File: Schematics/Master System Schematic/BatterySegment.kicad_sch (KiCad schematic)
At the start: 148 parts

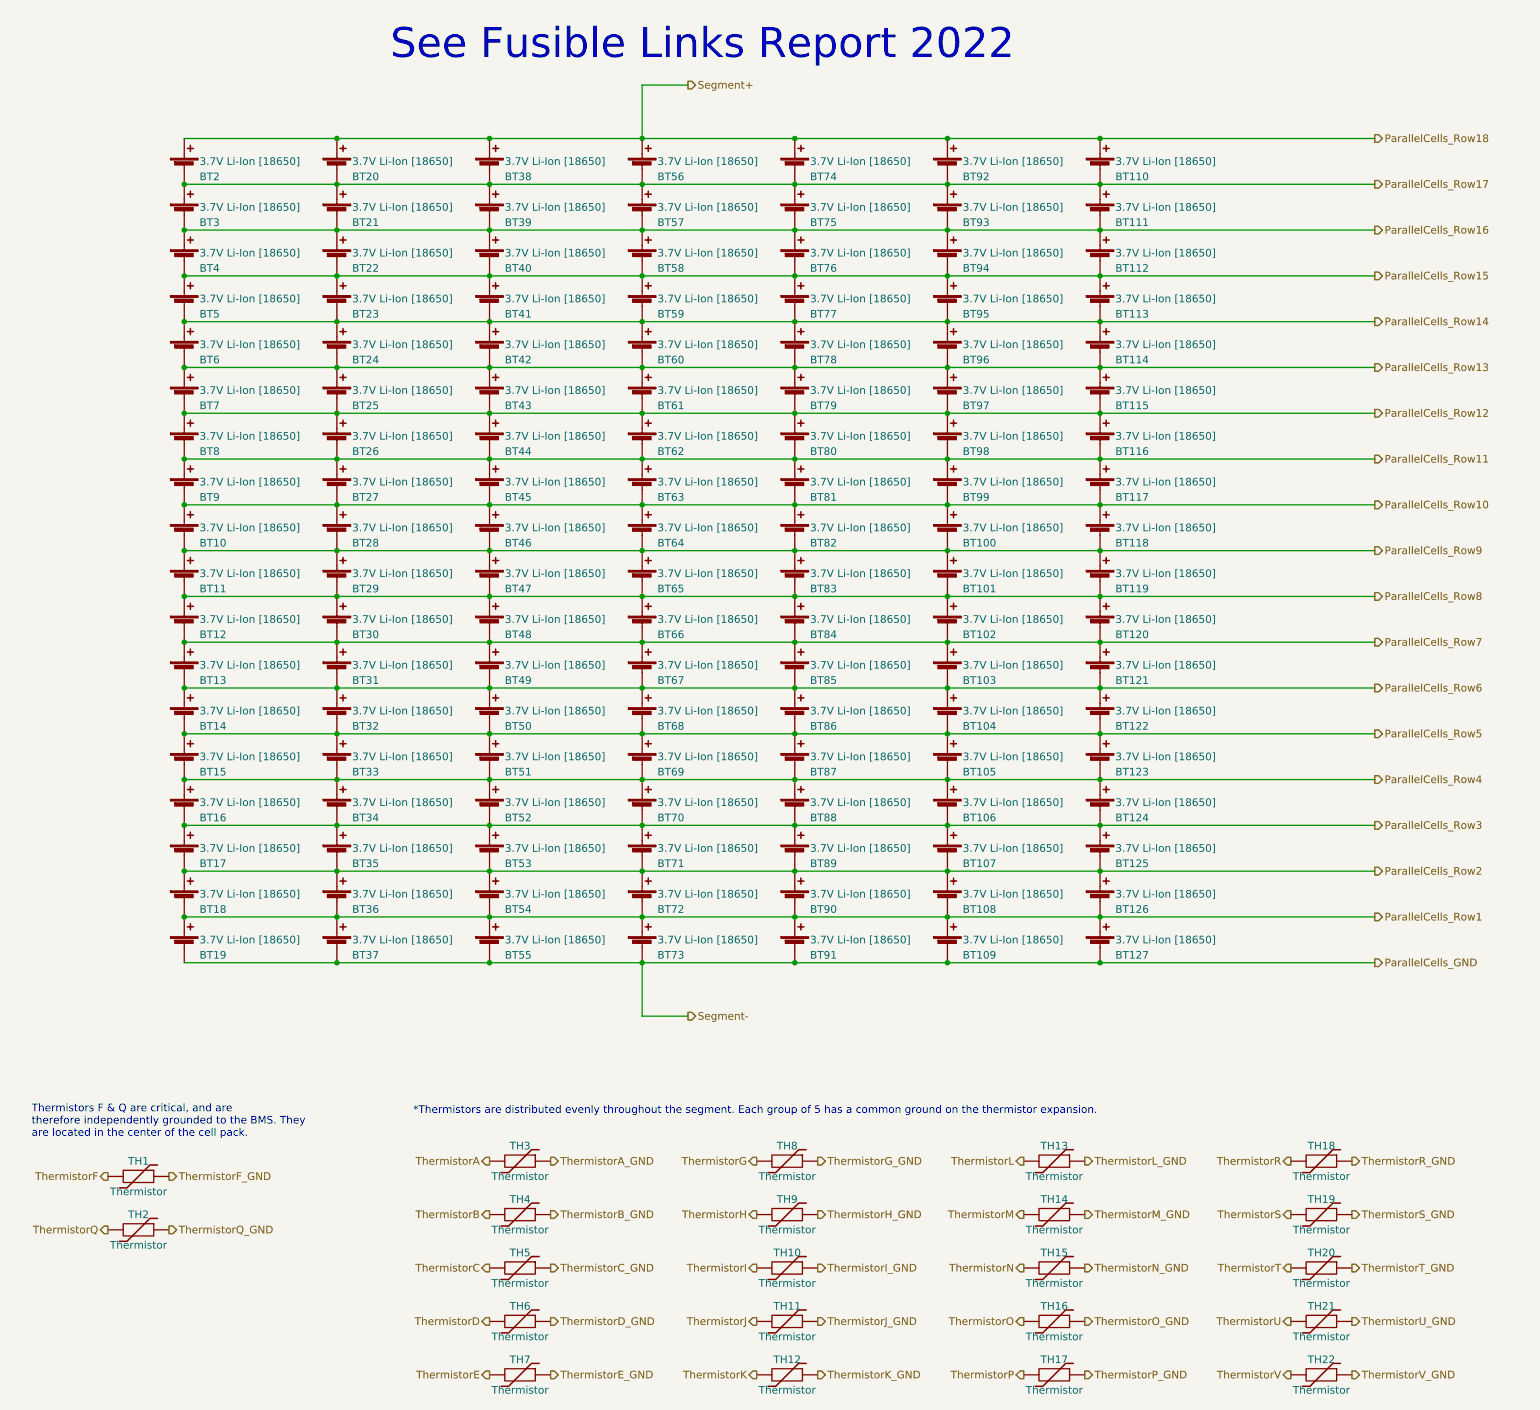
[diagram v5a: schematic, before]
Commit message: Update for color coding
Update for color coding
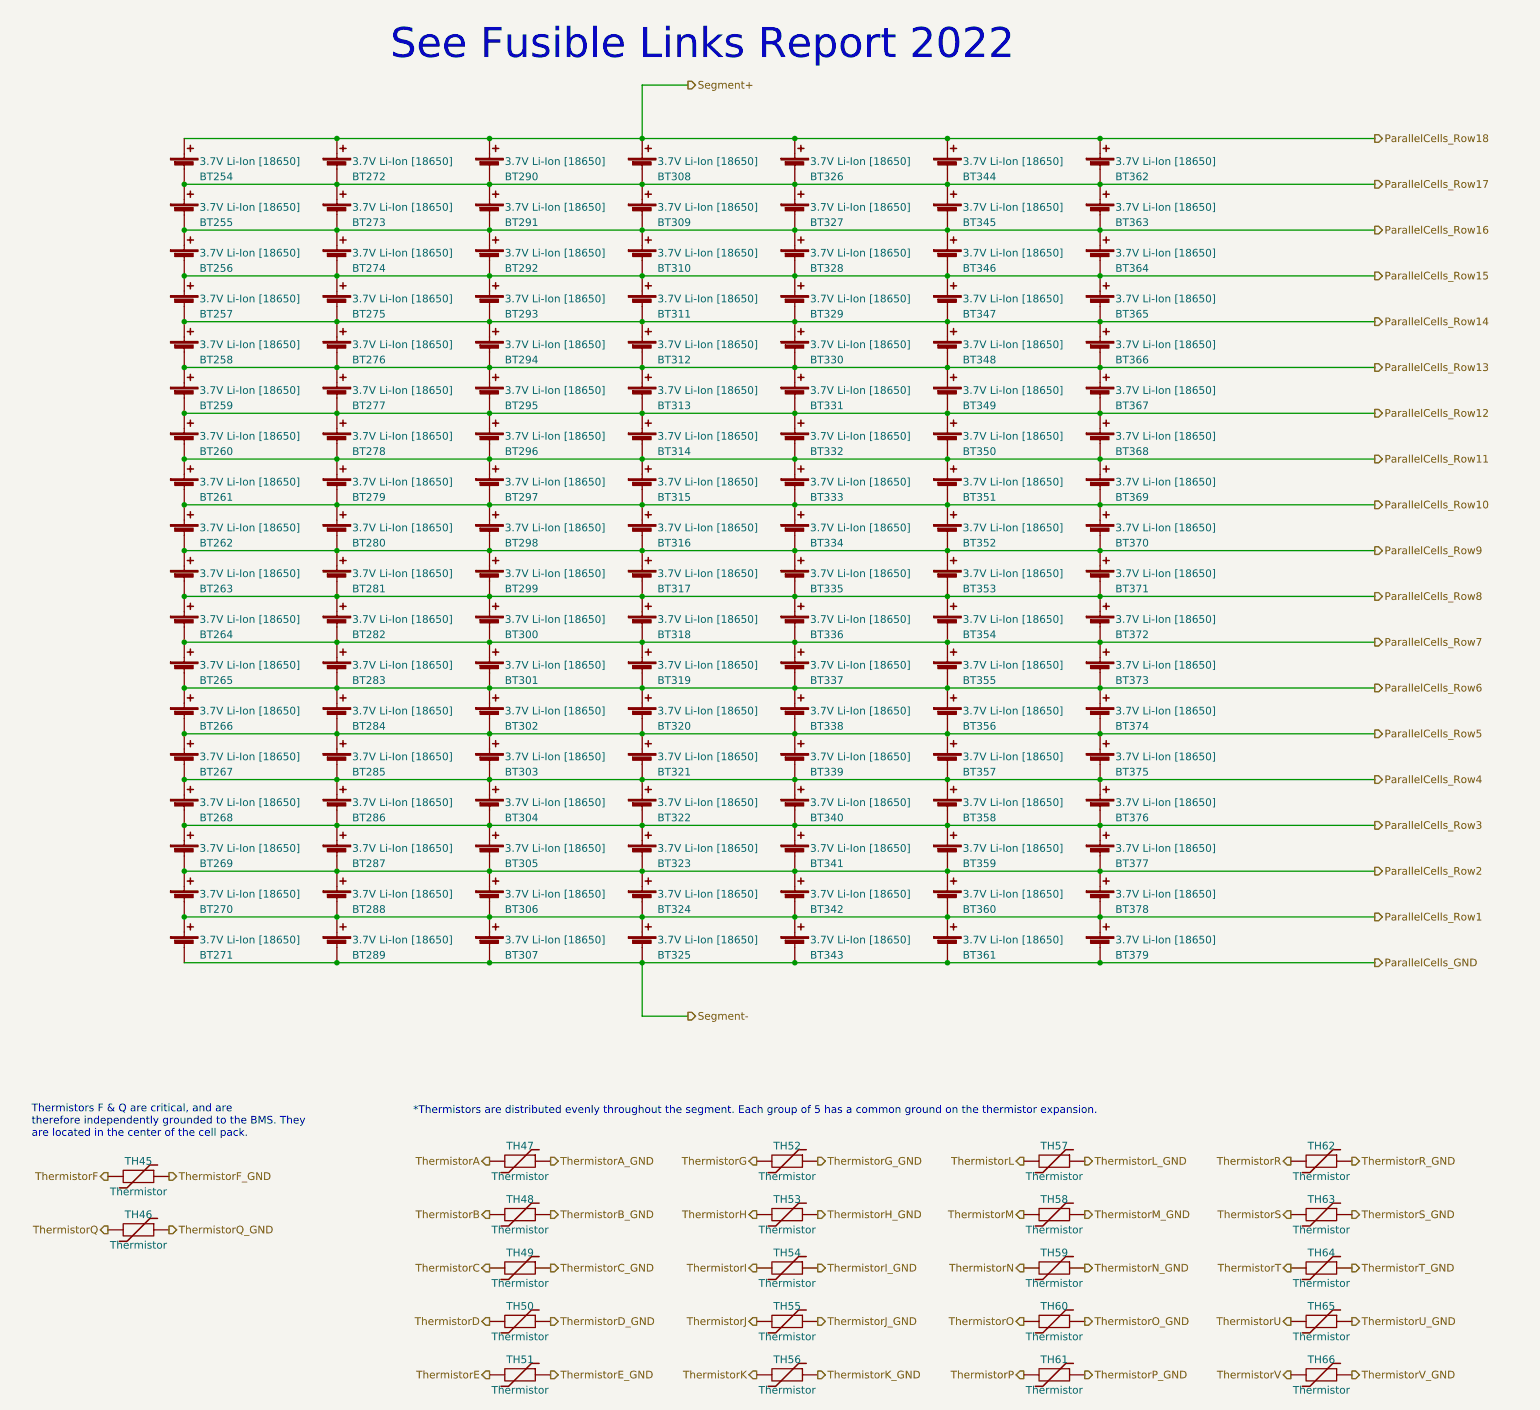
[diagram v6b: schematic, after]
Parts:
- renumbered BT2 to BT254, BT3 to BT255, BT4 to BT256, BT5 to BT257, BT6 to BT258, BT7 to BT259, BT8 to BT260, BT9 to BT261, BT10 to BT262, BT11 to BT263, BT12 to BT264, BT13 to BT265, BT14 to BT266, BT15 to BT267, BT16 to BT268, BT17 to BT269, BT18 to BT270, BT19 to BT271, BT20 to BT272, BT21 to BT273, BT22 to BT274, BT23 to BT275, BT24 to BT276, BT25 to BT277, BT26 to BT278, BT27 to BT279, BT28 to BT280, BT29 to BT281, BT30 to BT282, BT31 to BT283, BT32 to BT284, BT33 to BT285, BT34 to BT286, BT35 to BT287, BT36 to BT288, BT37 to BT289, BT38 to BT290, BT39 to BT291, BT40 to BT292, BT41 to BT293, BT42 to BT294, BT43 to BT295, BT44 to BT296, BT45 to BT297, BT46 to BT298, BT47 to BT299, BT48 to BT300, BT49 to BT301, BT50 to BT302, BT51 to BT303, BT52 to BT304, BT53 to BT305, BT54 to BT306, BT55 to BT307, BT56 to BT308, BT57 to BT309, BT58 to BT310, BT59 to BT311, BT60 to BT312, BT61 to BT313, BT62 to BT314, BT63 to BT315, BT64 to BT316, BT65 to BT317, BT66 to BT318, BT67 to BT319, BT68 to BT320, BT69 to BT321, BT70 to BT322, BT71 to BT323, BT72 to BT324, BT73 to BT325, BT74 to BT326, BT75 to BT327, BT76 to BT328, BT77 to BT329, BT78 to BT330, BT79 to BT331, BT80 to BT332, BT81 to BT333, BT82 to BT334, BT83 to BT335, BT84 to BT336, BT85 to BT337, BT86 to BT338, BT87 to BT339, BT88 to BT340, BT89 to BT341, BT90 to BT342, BT91 to BT343, BT92 to BT344, BT93 to BT345, BT94 to BT346, BT95 to BT347, BT96 to BT348, BT97 to BT349, BT98 to BT350, BT99 to BT351, BT100 to BT352, BT101 to BT353, BT102 to BT354, BT103 to BT355, BT104 to BT356, BT105 to BT357, BT106 to BT358, BT107 to BT359, BT108 to BT360, BT109 to BT361, BT110 to BT362, BT111 to BT363, BT112 to BT364, BT113 to BT365, BT114 to BT366, BT115 to BT367, BT116 to BT368, BT117 to BT369, BT118 to BT370, BT119 to BT371, BT120 to BT372, BT121 to BT373, BT122 to BT374, BT123 to BT375, BT124 to BT376, BT125 to BT377, BT126 to BT378, BT127 to BT379, TH1 to TH45, TH2 to TH46, TH3 to TH47, TH4 to TH48, TH5 to TH49, TH6 to TH50, TH7 to TH51, TH8 to TH52, TH9 to TH53, TH10 to TH54, TH11 to TH55, TH12 to TH56, TH13 to TH57, TH14 to TH58, TH15 to TH59, TH16 to TH60, TH17 to TH61, TH18 to TH62, TH19 to TH63, TH20 to TH64, TH21 to TH65, TH22 to TH66

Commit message: Charger and battbox stuff
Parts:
- renumbered BT262 to BT10, BT352 to BT100, BT353 to BT101, BT354 to BT102, BT355 to BT103, BT356 to BT104, BT357 to BT105, BT358 to BT106, BT359 to BT107, BT360 to BT108, BT361 to BT109, BT263 to BT11, BT362 to BT110, BT363 to BT111, BT364 to BT112, BT365 to BT113, BT366 to BT114, BT367 to BT115, BT368 to BT116, BT369 to BT117, BT370 to BT118, BT371 to BT119, BT264 to BT12, BT372 to BT120, BT373 to BT121, BT374 to BT122, BT375 to BT123, BT376 to BT124, BT377 to BT125, BT378 to BT126, BT379 to BT127, BT265 to BT13, BT266 to BT14, BT267 to BT15, BT268 to BT16, BT269 to BT17, BT270 to BT18, BT271 to BT19, BT254 to BT2, BT272 to BT20, BT273 to BT21, BT274 to BT22, BT275 to BT23, BT276 to BT24, BT277 to BT25, BT278 to BT26, BT279 to BT27, BT280 to BT28, BT281 to BT29, BT255 to BT3, BT282 to BT30, BT283 to BT31, BT284 to BT32, BT285 to BT33, BT286 to BT34, BT287 to BT35, BT288 to BT36, BT289 to BT37, BT290 to BT38, BT291 to BT39, BT256 to BT4, BT292 to BT40, BT293 to BT41, BT294 to BT42, BT295 to BT43, BT296 to BT44, BT297 to BT45, BT298 to BT46, BT299 to BT47, BT300 to BT48, BT301 to BT49, BT257 to BT5, BT302 to BT50, BT303 to BT51, BT304 to BT52, BT305 to BT53, BT306 to BT54, BT307 to BT55, BT308 to BT56, BT309 to BT57, BT310 to BT58, BT311 to BT59, BT258 to BT6, BT312 to BT60, BT313 to BT61, BT314 to BT62, BT315 to BT63, BT316 to BT64, BT317 to BT65, BT318 to BT66, BT319 to BT67, BT320 to BT68, BT321 to BT69, BT259 to BT7, BT322 to BT70, BT323 to BT71, BT324 to BT72, BT325 to BT73, BT326 to BT74, BT327 to BT75, BT328 to BT76, BT329 to BT77, BT330 to BT78, BT331 to BT79, BT260 to BT8, BT332 to BT80, BT333 to BT81, BT334 to BT82, BT335 to BT83, BT336 to BT84, BT337 to BT85, BT338 to BT86, BT339 to BT87, BT340 to BT88, BT341 to BT89, BT261 to BT9, BT342 to BT90, BT343 to BT91, BT344 to BT92, BT345 to BT93, BT346 to BT94, BT347 to BT95, BT348 to BT96, BT349 to BT97, BT350 to BT98, BT351 to BT99, TH45 to TH1, TH54 to TH10, TH55 to TH11, TH56 to TH12, TH57 to TH13, TH58 to TH14, TH59 to TH15, TH60 to TH16, TH61 to TH17, TH62 to TH18, TH63 to TH19, TH46 to TH2, TH64 to TH20, TH65 to TH21, TH66 to TH22, TH47 to TH3, TH48 to TH4, TH49 to TH5, TH50 to TH6, TH51 to TH7, TH52 to TH8, TH53 to TH9

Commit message: Annotations
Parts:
- renumbered BT2 to BT1479, BT3 to BT1480, BT4 to BT1481, BT5 to BT1482, BT6 to BT1483, BT7 to BT1484, BT8 to BT1485, BT9 to BT1486, BT10 to BT1487, BT11 to BT1488, BT12 to BT1489, BT13 to BT1490, BT14 to BT1491, BT15 to BT1492, BT16 to BT1493, BT17 to BT1494, BT18 to BT1495, BT19 to BT1496, BT20 to BT1497, BT21 to BT1498, BT22 to BT1499, BT23 to BT1500, BT24 to BT1501, BT25 to BT1502, BT26 to BT1503, BT27 to BT1504, BT28 to BT1505, BT29 to BT1506, BT30 to BT1507, BT31 to BT1508, BT32 to BT1509, BT33 to BT1510, BT34 to BT1511, BT35 to BT1512, BT36 to BT1513, BT37 to BT1514, BT38 to BT1515, BT39 to BT1516, BT40 to BT1517, BT41 to BT1518, BT42 to BT1519, BT43 to BT1520, BT44 to BT1521, BT45 to BT1522, BT46 to BT1523, BT47 to BT1524, BT48 to BT1525, BT49 to BT1526, BT50 to BT1527, BT51 to BT1528, BT52 to BT1529, BT53 to BT1530, BT54 to BT1531, BT55 to BT1532, BT56 to BT1533, BT57 to BT1534, BT58 to BT1535, BT59 to BT1536, BT60 to BT1537, BT61 to BT1538, BT62 to BT1539, BT63 to BT1540, BT64 to BT1541, BT65 to BT1542, BT66 to BT1543, BT67 to BT1544, BT68 to BT1545, BT69 to BT1546, BT70 to BT1547, BT71 to BT1548, BT72 to BT1549, BT73 to BT1550, BT74 to BT1551, BT75 to BT1552, BT76 to BT1553, BT77 to BT1554, BT78 to BT1555, BT79 to BT1556, BT80 to BT1557, BT81 to BT1558, BT82 to BT1559, BT83 to BT1560, BT84 to BT1561, BT85 to BT1562, BT86 to BT1563, BT87 to BT1564, BT88 to BT1565, BT89 to BT1566, BT90 to BT1567, BT91 to BT1568, BT92 to BT1569, BT93 to BT1570, BT94 to BT1571, BT95 to BT1572, BT96 to BT1573, BT97 to BT1574, BT98 to BT1575, BT99 to BT1576, BT100 to BT1577, BT101 to BT1578, BT102 to BT1579, BT103 to BT1580, BT104 to BT1581, BT105 to BT1582, BT106 to BT1583, BT107 to BT1584, BT108 to BT1585, BT109 to BT1586, BT110 to BT1587, BT111 to BT1588, BT112 to BT1589, BT113 to BT1590, BT114 to BT1591, BT115 to BT1592, BT116 to BT1593, BT117 to BT1594, BT118 to BT1595, BT119 to BT1596, BT120 to BT1597, BT121 to BT1598, BT122 to BT1599, BT123 to BT1600, BT124 to BT1601, BT125 to BT1602, BT126 to BT1603, BT127 to BT1604, TH1 to TH1401, TH2 to TH1402, TH3 to TH1403, TH4 to TH1404, TH5 to TH1405, TH6 to TH1406, TH7 to TH1407, TH8 to TH1408, TH9 to TH1409, TH10 to TH1410, TH11 to TH1411, TH12 to TH1412, TH13 to TH1413, TH14 to TH1414, TH15 to TH1415, TH16 to TH1416, TH17 to TH1417, TH18 to TH1418, TH19 to TH1419, TH20 to TH1420, TH21 to TH1421, TH22 to TH1422
